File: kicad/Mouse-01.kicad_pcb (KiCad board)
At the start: 2 copper layers, 54 x 62 mm, 89 parts, among them P1 MT-ENC, P2 MT-ENC, P3 Battery_A, P4 Battery_B, P5 SWD, P6 UART, Q1 IRLML6402, Q2 IRFML8244, Q3 IRFML8244, Q4 BSS138, SW1 RESET, SW2 Power, SW3 BUTTON, U1 STM32F405RGTx, U2 DRV8835, U3 DRV8835, U4 LXDC55FAAA-203, U5 REF1933, U6 LT1963ES8, U7 AD8604, U8 MPU6500

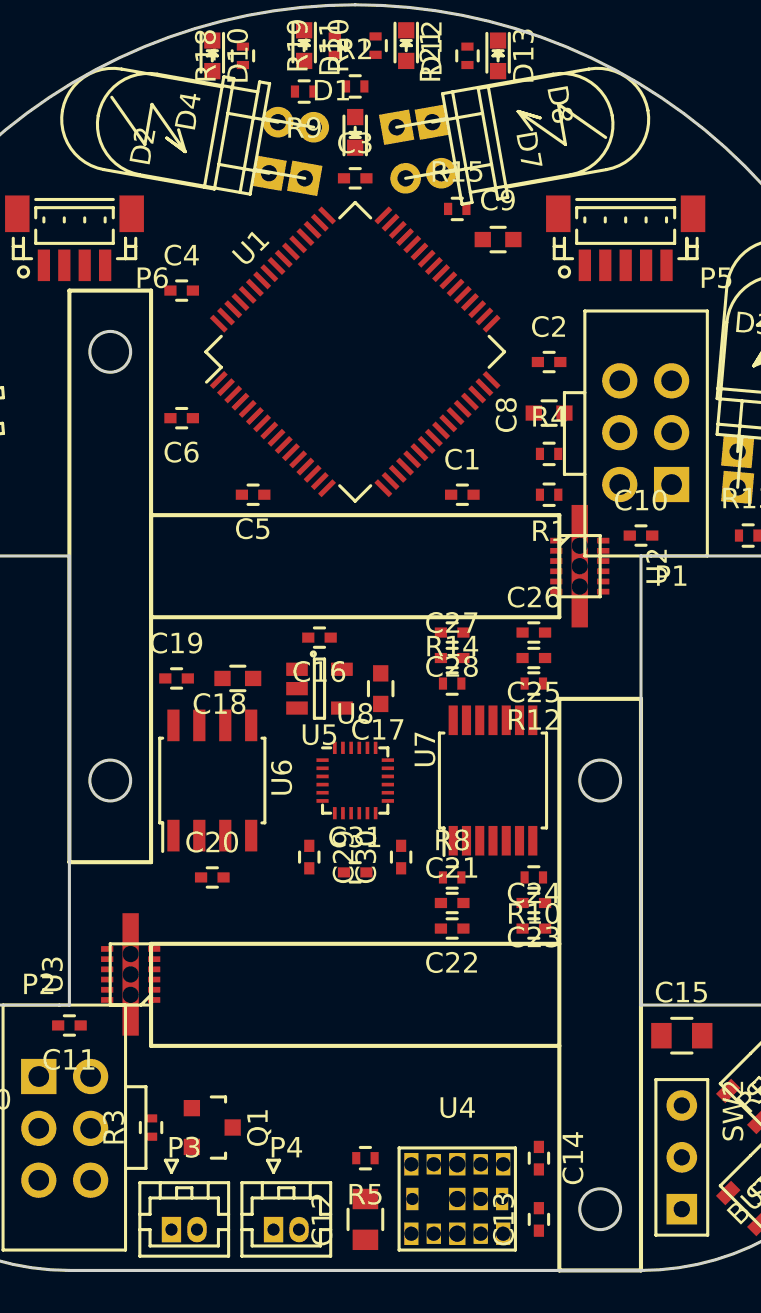
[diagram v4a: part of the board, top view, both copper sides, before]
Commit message: ネットリストを更新
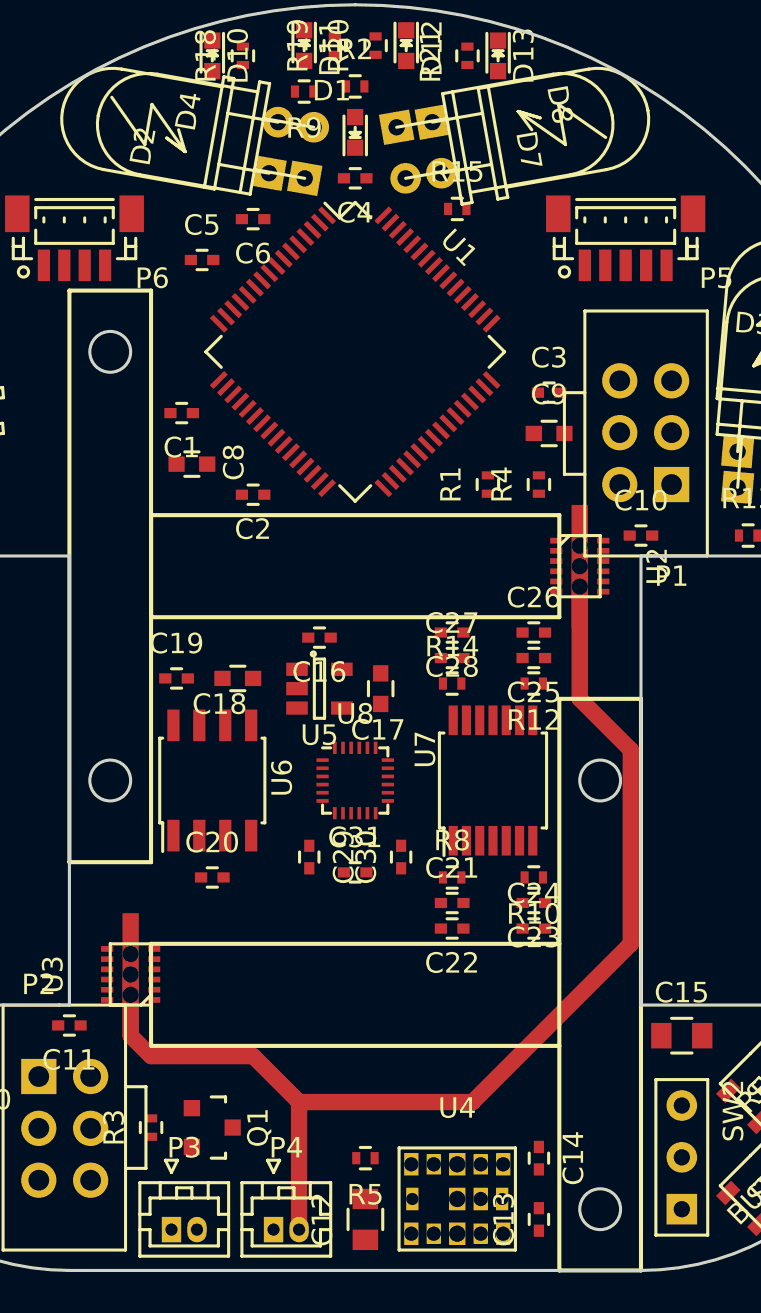
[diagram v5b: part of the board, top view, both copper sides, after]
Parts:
- moved C8 17.7 mm to (135.0, 118.5), turned to 180 degrees
- moved C2 15.9 mm to (138.0, 120.0), turned to 180 degrees
- moved C1 14.3 mm to (134.5, 116.0), turned to 180 degrees
- moved C3 14.2 mm to (152.5, 115.0)
- moved C5 11.8 mm to (135.5, 108.5), turned to 0 degrees
- moved C6 10.4 mm to (138.0, 106.5)
- moved C4 10.1 mm to (143.0, 104.5), turned to 180 degrees
- moved C9 9.82 mm to (152.5, 117.0)
- moved R1 3.04 mm to (149.5, 119.5), turned to 90 degrees
- moved R4 1.58 mm to (152.0, 119.5), turned to 90 degrees
- turned U1 to 315 degrees
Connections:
- net Net-(P3-Pad1) renamed /Power/BAT_to_FET
- net Net-(P3-Pad2) renamed /Power/BAT_to_BAT
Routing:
- net GND: track 0.00 -> 57.8 mm
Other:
- net class 3.3V: trace_width 0.29 -> 0.3
- net class 5V: trace_width 0.44 -> 0.4; via_dia 0.6 -> 0.5
- net class AXIS: trace_width 0.19 -> 0.2
- net class GND: trace_width 0.44 -> 0.4; via_dia 0.6 -> 0.5
- net class IR_LED: trace_width 0.44 -> 0.4; via_dia 0.6 -> 0.5
- net class Motor: via_drill 0.6 -> 0.8
- net class VBAT: via_drill 0.6 -> 0.8

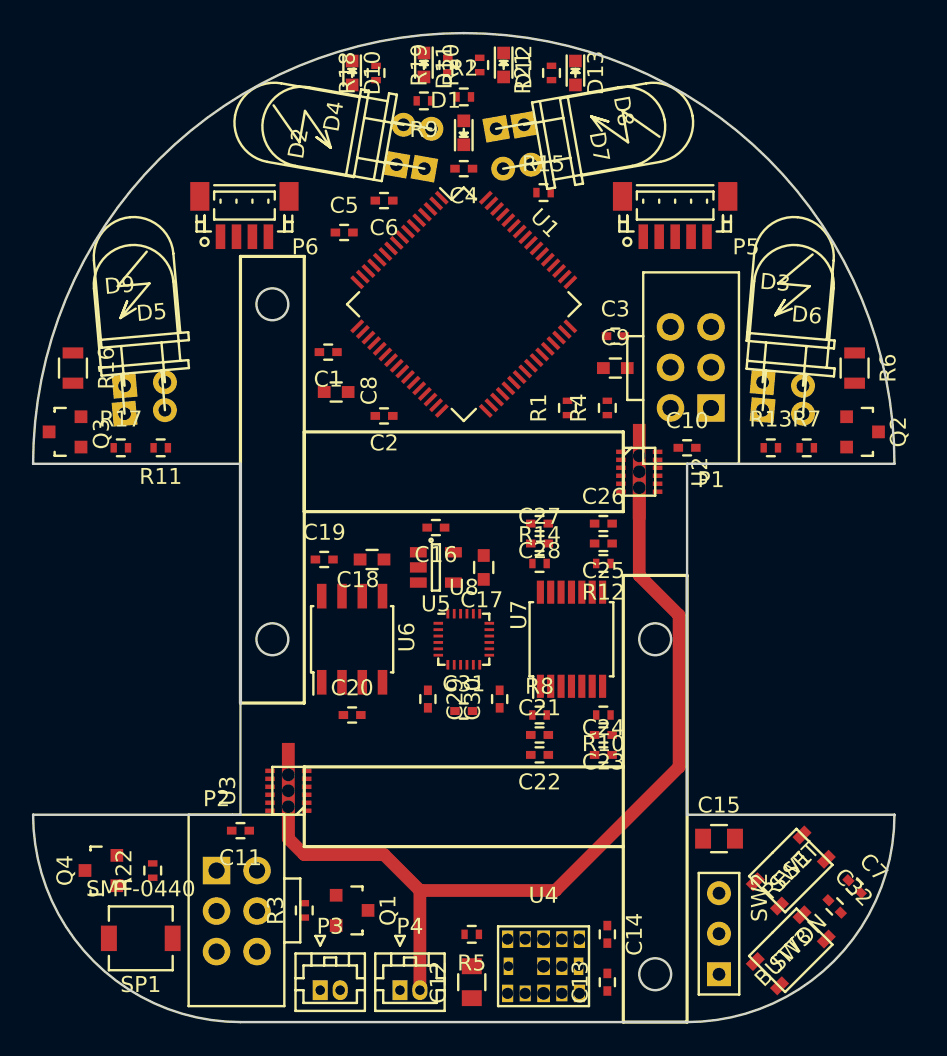
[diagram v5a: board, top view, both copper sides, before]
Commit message: IR LEDとフォトダイオードのフットプリントを更新．
かなりすっきり収まった．
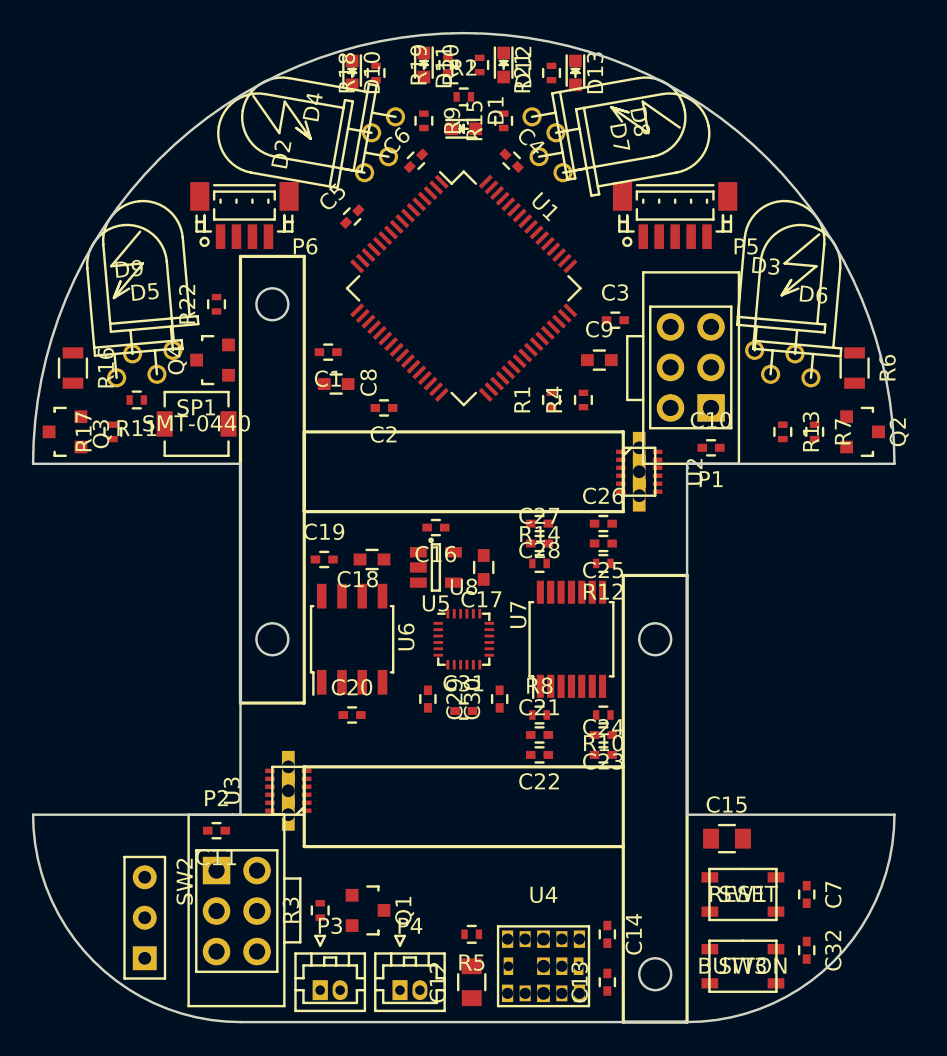
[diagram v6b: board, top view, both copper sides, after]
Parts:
- moved SW2 36.0 mm to (123.0, 154.0)
- moved R22 35.7 mm to (127.5, 113.0)
- moved Q4 32.8 mm to (127.2, 116.5)
- moved SP1 32.4 mm to (126.2, 120.5), turned to 0 degrees
- moved R15 5.15 mm to (145.5, 101.5), turned to 90 degrees
- moved R11 3.35 mm to (122.5, 119.0)
- moved SW1 3.35 mm to (160.5, 150.0), turned to 0 degrees
- moved C32 3.26 mm to (164.5, 153.5), turned to 270 degrees
- moved C6 3.20 mm to (140.0, 104.0), turned to 45 degrees
- moved SW3 3.16 mm to (160.5, 154.5), turned to 0 degrees
- moved C4 3.04 mm to (146.0, 104.0), turned to 315 degrees
- moved C7 3.04 mm to (164.5, 150.0), turned to 270 degrees
- moved D4 2.37 mm to (138.5, 102.5)
- moved D7 2.37 mm to (147.5, 102.5)
- moved D5 2.30 mm to (122.5, 117.5)
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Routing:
- net GND: track 57.8 -> 0.00 mm
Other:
- net class GND: trace_width 0.4 -> 0.8

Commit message: 部品の位置を調整，ロゴを貼り付け
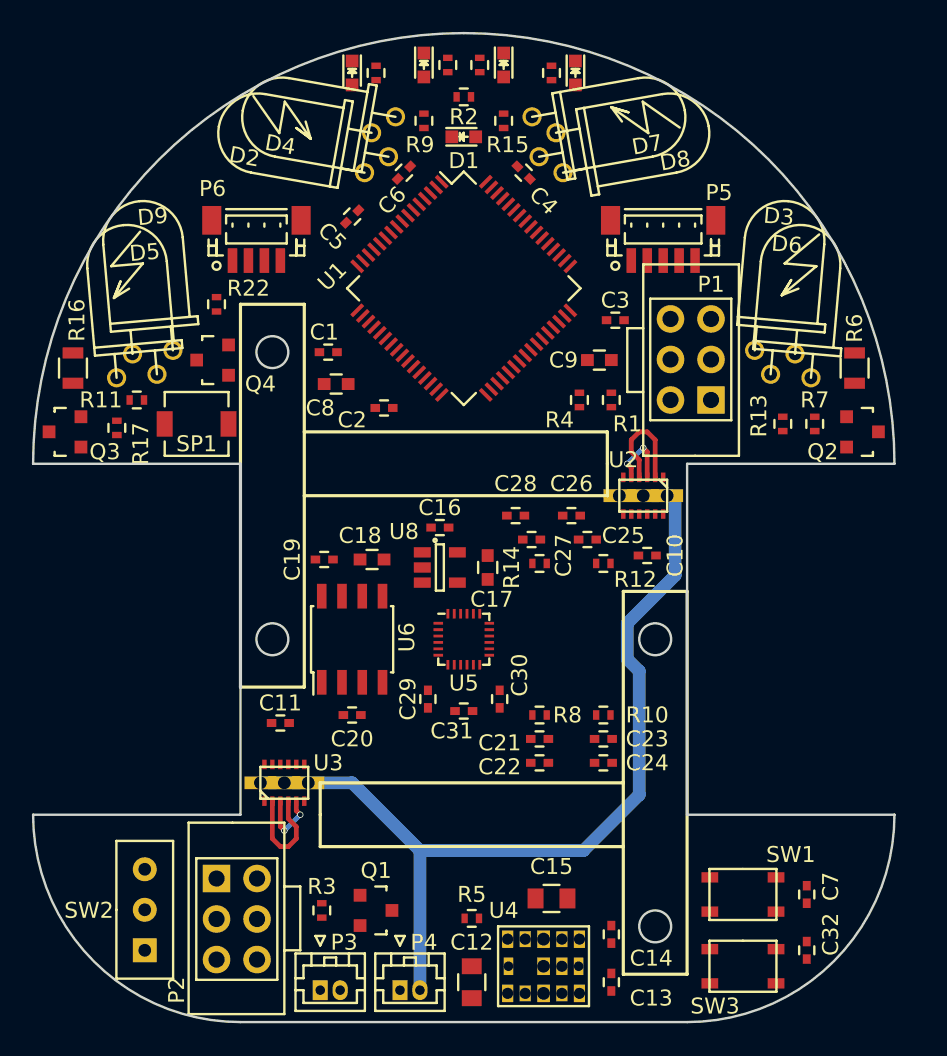
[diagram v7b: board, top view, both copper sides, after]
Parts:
- removed U7: AD8604, Housings_SSOP:TSSOP-14_4.4x5mm_Pitch0.65mm
- added G***: LOGO, KERI:KERI_22mm, B.Cu at (143.0, 131.0)
- moved C15 11.6 mm to (148.5, 150.2)
- moved C10 7.85 mm to (154.5, 128.8), turned to 180 degrees
- moved C11 7.85 mm to (131.5, 139.2), turned to 0 degrees
- moved R1 3.75 mm to (152.2, 119.0)
- moved C26 2.06 mm to (149.8, 126.2)
- moved P5 1.68 mm to (155.5, 109.0)
- moved P6 1.68 mm to (130.0, 109.0)
- moved C28 1.58 mm to (146.2, 126.2)
- moved U2 1.52 mm to (154.2, 125.0), turned to 180 degrees
- moved C4 1.06 mm to (146.8, 104.8)
- moved C6 1.06 mm to (139.2, 104.8), turned to 225 degrees
- moved C25 1.03 mm to (150.8, 127.8)
- moved R5 1.00 mm to (143.5, 151.5)
- moved C27 0.56 mm to (147.2, 127.8)
- moved U3 0.56 mm to (131.8, 143.0), turned to 0 degrees
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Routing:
- net GND: track 0.00 -> 57.9 mm
- net /Motor_R/MT_OUT_1: track 0.00 -> 6.82 mm
- net /Motor_L/MT_OUT_1: track 0.00 -> 6.82 mm
- net /Motor_R/MT_OUT_2: track 0.00 -> 4.32 mm, vias 0 -> 2
- net /Motor_L/MT_OUT_2: track 0.00 -> 4.32 mm, vias 0 -> 2
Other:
- outline, holes or cut-outs redrawn
- net class 3.3V: trace_width 0.3 -> 0.2999
- net class Default: trace_width 0.2 -> 0.1999
- net class GND: trace_width 0.8 -> 0.4
- board text added: "kerikun11 2016.12.01"

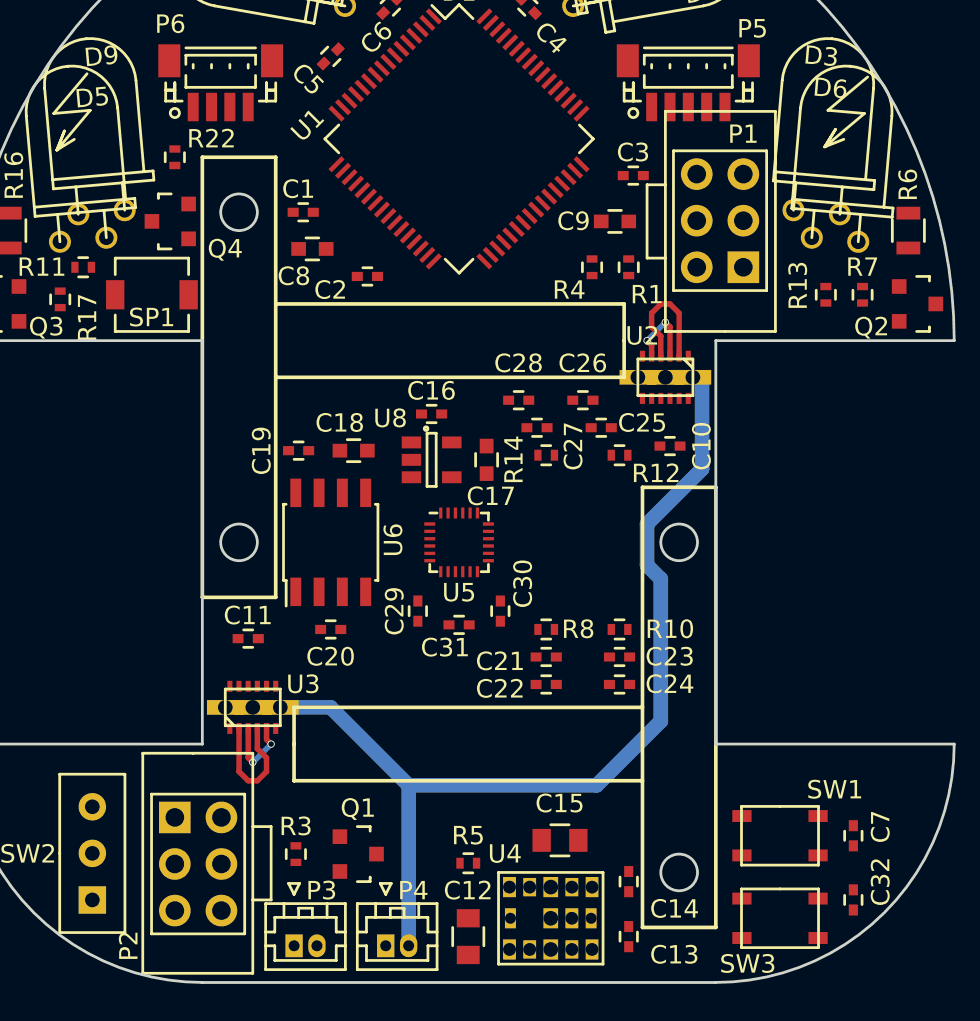
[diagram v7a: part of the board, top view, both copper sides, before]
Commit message: 自動配線へ出力
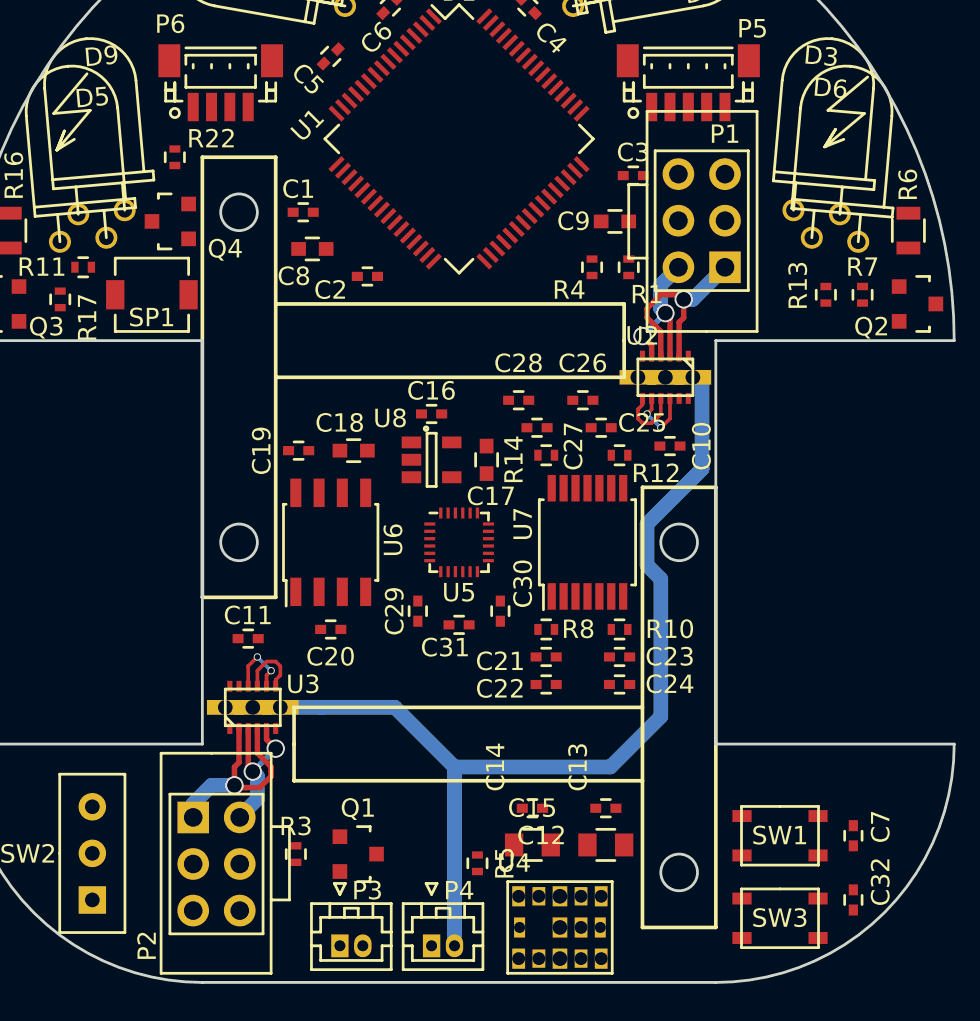
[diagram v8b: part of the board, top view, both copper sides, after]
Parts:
- removed G***: LOGO, KERI:KERI_22mm
- added U7: AD8604, Housings_SSOP:TSSOP-14_4.4x5mm_Pitch0.65mm, F.Cu at (150.0, 134.0)
- moved C12 9.01 mm to (151.0, 150.5), turned to 180 degrees
- moved C13 7.11 mm to (151.0, 148.5), turned to 180 degrees
- moved C14 6.60 mm to (147.0, 148.5), turned to 0 degrees
- moved P3 2.50 mm to (136.5, 156.0)
- moved P4 2.50 mm to (141.5, 156.0)
- moved C15 1.52 mm to (147.0, 150.5)
- moved P1 1.00 mm to (157.5, 119.0)
- moved P2 1.00 mm to (128.5, 149.0)
- moved U4 0.71 mm to (148.5, 155.0)
- moved R5 0.50 mm to (144.0, 151.5), turned to 90 degrees
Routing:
- net /Motor_R/MT_OUT_1: track 6.82 -> 11.8 mm, vias 0 -> 1
- net /Motor_L/MT_OUT_1: track 6.82 -> 11.5 mm, vias 0 -> 1
- net /Motor_L/MT_OUT_2: track 4.32 -> 8.55 mm
- net /Motor_R/MT_OUT_2: track 4.32 -> 8.53 mm
- net MT-IN-R-1: track 0.00 -> 3.82 mm, vias 0 -> 2
- net MT-IN-L-1: track 0.00 -> 3.82 mm, vias 0 -> 2
- net MT-IN-R-2: track 0.00 -> 3.61 mm
- net MT-IN-L-2: track 0.00 -> 3.61 mm
